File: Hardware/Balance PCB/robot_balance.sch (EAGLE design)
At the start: 49 parts, among them Q1 16Mhz

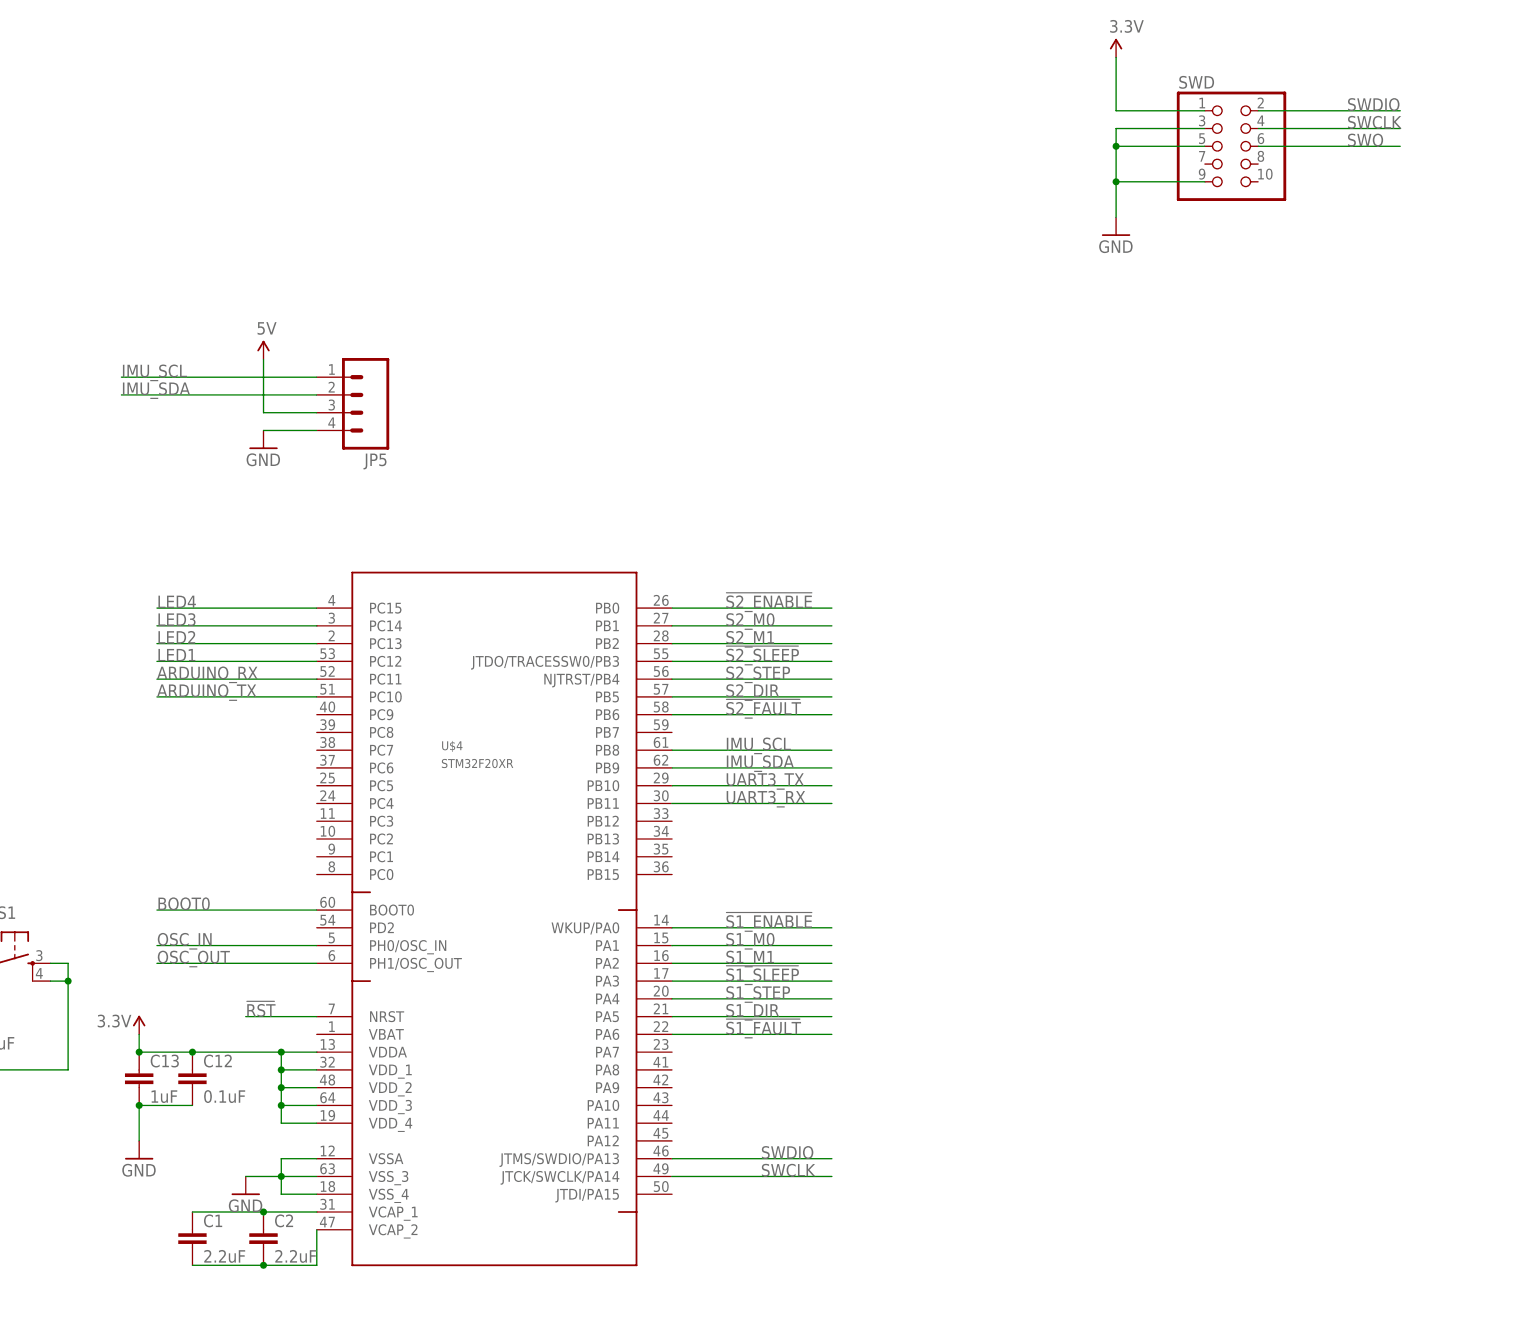
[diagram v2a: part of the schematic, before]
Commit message: Put a larger JTAG connector
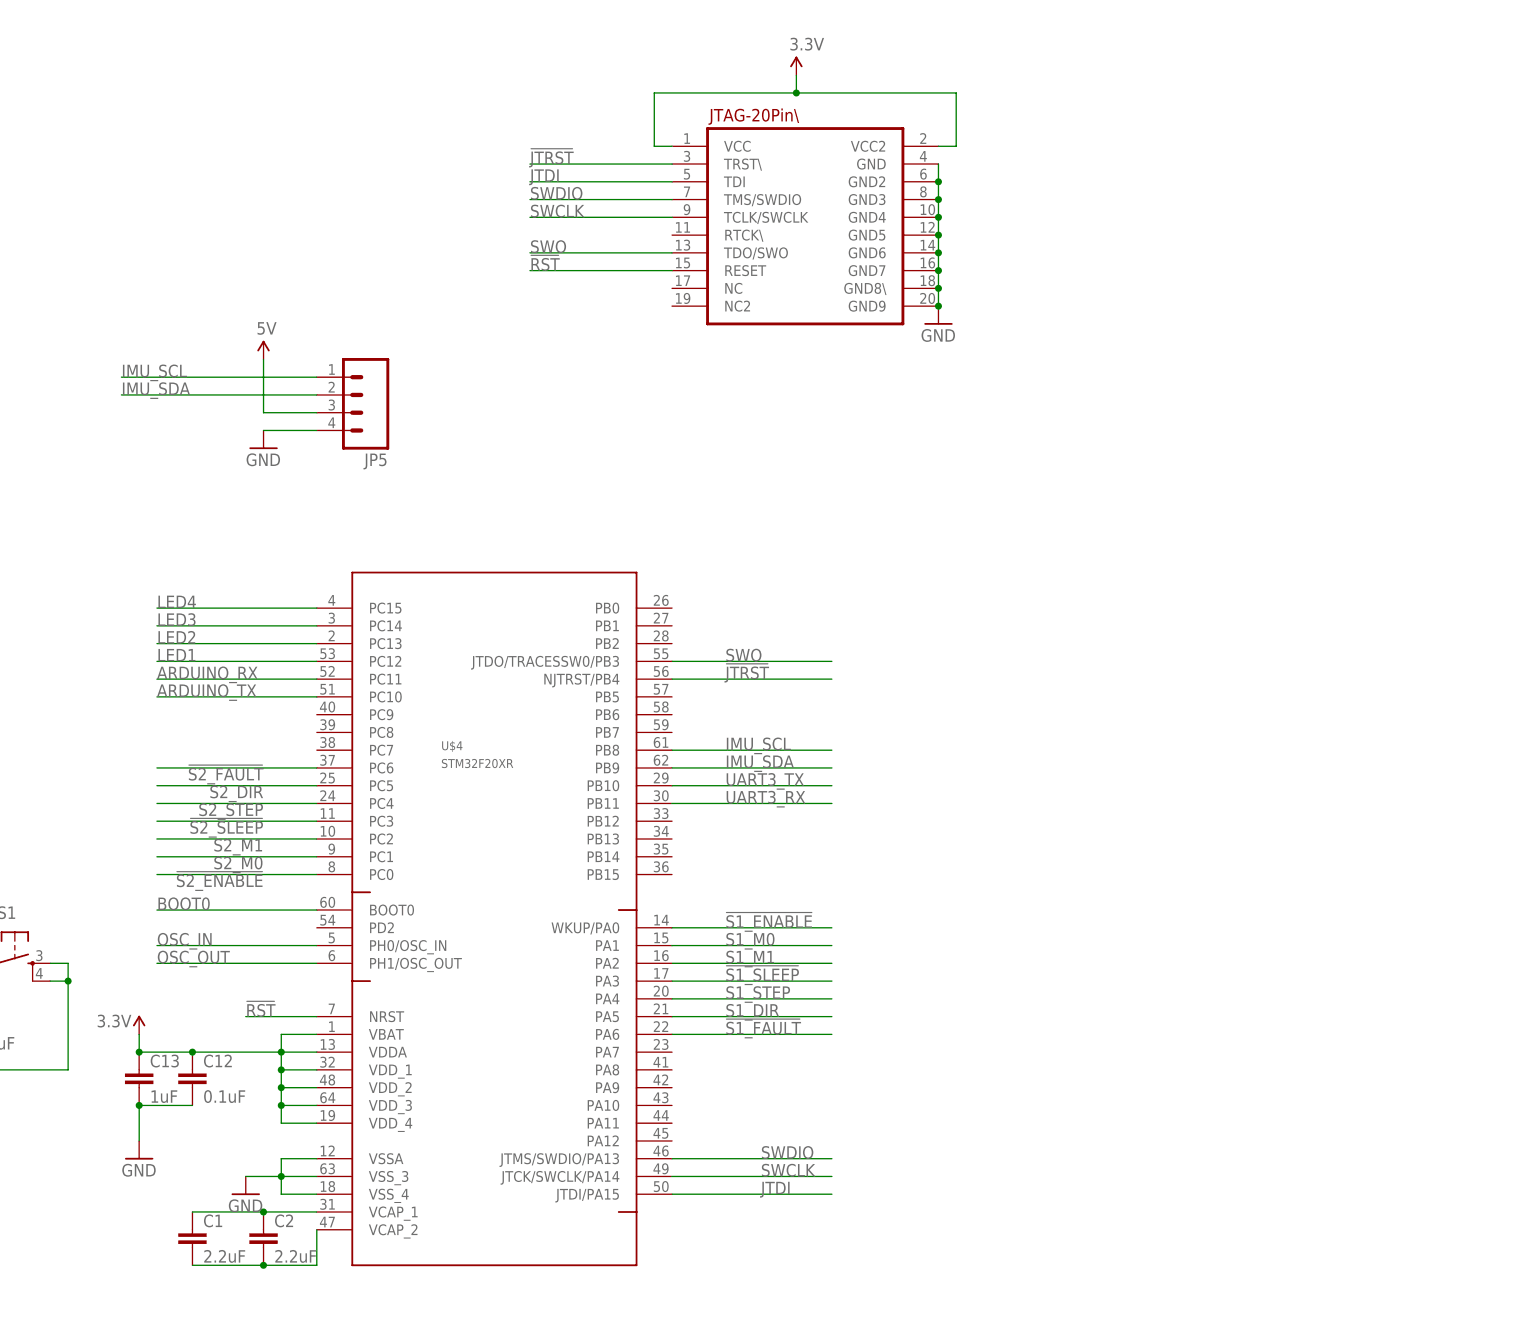
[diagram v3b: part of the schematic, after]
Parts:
- removed SWD: (no value), Sandwich:PINHD-2X5-1.27MM
- added U$2: JTAG_20PIN, JonathanLukas:JTAG_20PIN
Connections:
- new net !JTRST: U$2.TRST\, U$4.NJTRST/PB4
- new net JTDI: U$2.TDI, U$4.JTDI/PA15
- net !RST: now also U$2.RESET
- net !S2_ENABLE: now also U$4.PC0; no longer U$4.PB0
- net !S2_FAULT: now also U$4.PC6; no longer U$4.PB6
- net !S2_SLEEP: now also U$4.PC3; no longer U$4.JTDO/TRACESSW0/PB3
- net 3.3V: now also U$2.VCC, U$2.VCC2, U$4.VBAT; no longer SWD.1
- net GND: now also U$2.GND, U$2.GND2, U$2.GND3, U$2.GND4, U$2.GND5, U$2.GND6, U$2.GND7, U$2.GND8\, U$2.GND9; no longer SWD.3, SWD.5, SWD.9
- net S2_DIR: now also U$4.PC5; no longer U$4.PB5
- net S2_M0: now also U$4.PC1; no longer U$4.PB1
- net S2_M1: now also U$4.PC2; no longer U$4.PB2
- net S2_STEP: now also U$4.PC4; no longer U$4.NJTRST/PB4
- net SWCLK: now also U$2.TCLK/SWCLK; no longer SWD.4
- net SWDIO: now also U$2.TMS/SWDIO; no longer SWD.2
- net SWO: now also U$2.TDO/SWO, U$4.JTDO/TRACESSW0/PB3; no longer SWD.6

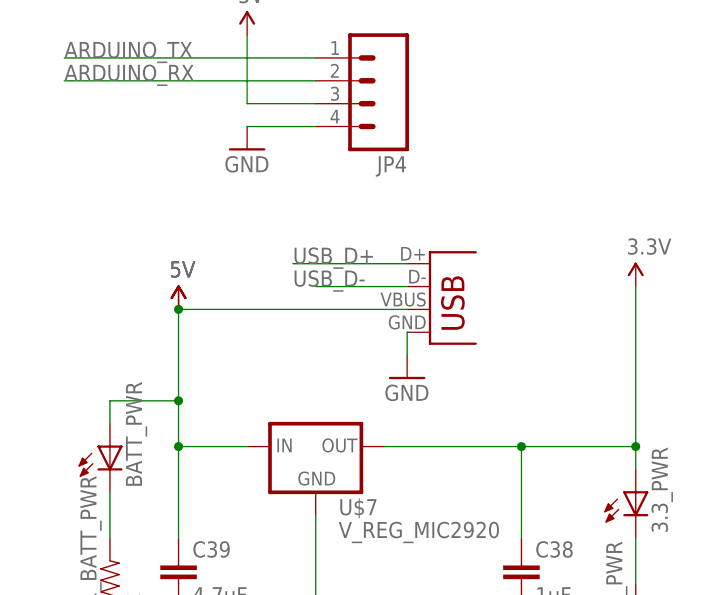
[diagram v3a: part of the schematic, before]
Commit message: Micro usb instead of Mini
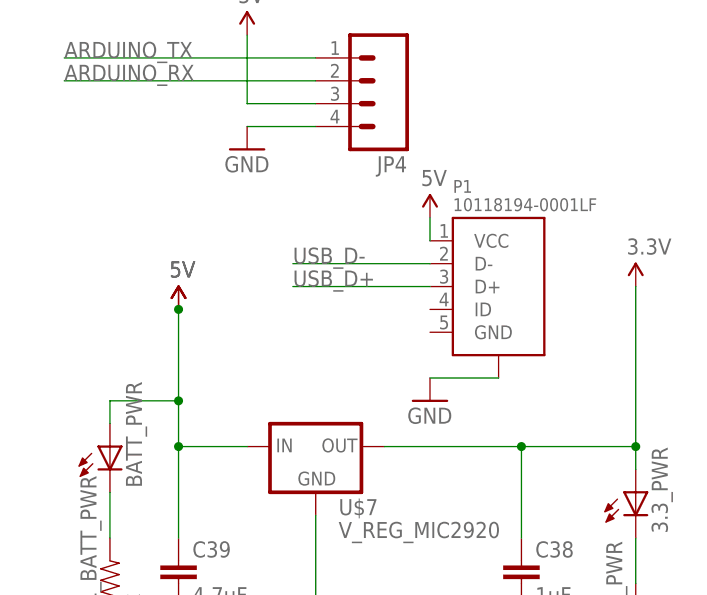
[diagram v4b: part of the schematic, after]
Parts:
- removed JP3: USBOLD, SparkFun-Connectors:USBOLD
- added P1: 10118194-0001LF, usb_micro:10118194-0001LF
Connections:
- net 5V: now also P1.VCC; no longer JP3.VBUS
- net GND: now also P1.SHIELD; no longer JP3.GND
- net USB_D+: now also P1.D+; no longer JP3.D+
- net USB_D-: now also P1.D-; no longer JP3.D-
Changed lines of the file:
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@@
 <part name="GND5" library="SparkFun-Aesthetics" deviceset="GND" device=""/>
 <part name="C4" library="SparkFun-Capacitors" deviceset="47UF-10V-10%(TANT)" device="" value="47uF"/>
-<part name="JP3" library="SparkFun-Connectors" deviceset="USB" device="OLD"/>
 <part name="GND6" library="SparkFun-Aesthetics" deviceset="GND" device=""/>
 <part name="JP4" library="SparkFun-Connectors" deviceset="M04" device="POLAR_LOCK"/>
@@
 <part name="GND12" library="SparkFun-Aesthetics" deviceset="GND" device=""/>
 <part name="SUPPLY9" library="SparkFun-Aesthetics" deviceset="3.3V" device=""/>
+<part name="P1" library="usb_micro" deviceset="10118194-0001LF" device=""/>
+<part name="SUPPLY13" library="SparkFun-Aesthetics" deviceset="5V" device=""/>
 </parts>
 <sheets>
@@
 <instance part="GND5" gate="1" x="335.28" y="-17.78"/>
 <instance part="C4" gate="G$1" x="317.5" y="-10.16"/>
-<instance part="JP3" gate="G$1" x="312.42" y="-132.08"/>
-<instance part="GND6" gate="1" x="309.88" y="-137.16"/>
+<instance part="GND6" gate="1" x="312.42" y="-139.7"/>
 <instance part="JP4" gate="G$1" x="304.8" y="-104.14" rot="R180"/>
 <instance part="GND7" gate="1" x="292.1" y="-111.76"/>
@@
 <instance part="GND12" gate="1" x="154.94" y="43.18"/>
 <instance part="SUPPLY9" gate="G$1" x="134.62" y="78.74"/>
+<instance part="P1" gate="G$1" x="317.5" y="-127"/>
+<instance part="SUPPLY13" gate="G$1" x="312.42" y="-119.38"/>
 </instances>
 <busses>
@@
 </segment>
 <segment>
-<pinref part="JP3" gate="G$1" pin="GND"/>
 <pinref part="GND6" gate="1" pin="GND"/>
-<wire x1="309.88" y1="-134.62" x2="309.88" y2="-132.08" width="0.1524" layer="91"/>
+<wire x1="312.42" y1="-137.16" x2="320.04" y2="-137.16" width="0.1524" layer="91"/>
+<pinref part="P1" gate="G$1" pin="SHIELD"/>
 </segment>
 <segment>
@@
 </segment>
 <segment>
-<wire x1="299.72" y1="-127" x2="309.88" y2="-127" width="0.1524" layer="91"/>
-<label x="297.18" y="-127" size="1.778" layer="95"/>
-<pinref part="JP3" gate="G$1" pin="D-"/>
+<wire x1="297.18" y1="-124.46" x2="312.42" y2="-124.46" width="0.1524" layer="91"/>
+<label x="297.18" y="-124.46" size="1.778" layer="95"/>
+<pinref part="P1" gate="G$1" pin="D-"/>
 </segment>
 </net>
@@
 </segment>
 <segment>
-<wire x1="297.18" y1="-124.46" x2="309.88" y2="-124.46" width="0.1524" layer="91"/>
-<label x="297.18" y="-124.46" size="1.778" layer="95"/>
-<pinref part="JP3" gate="G$1" pin="D+"/>
+<wire x1="297.18" y1="-127" x2="312.42" y2="-127" width="0.1524" layer="91"/>
+<label x="297.18" y="-127" size="1.778" layer="95"/>
+<pinref part="P1" gate="G$1" pin="D+"/>
 </segment>
 </net>
@@
 <wire x1="284.48" y1="-154.94" x2="284.48" y2="-144.78" width="0.1524" layer="91"/>
 <junction x="284.48" y="-144.78"/>
-<pinref part="JP3" gate="G$1" pin="VBUS"/>
-<wire x1="309.88" y1="-129.54" x2="284.48" y2="-129.54" width="0.1524" layer="91"/>
 <pinref part="SUPPLY5" gate="G$1" pin="5V"/>
 <junction x="284.48" y="-129.54"/>
@@
 <pinref part="SUPPLY6" gate="G$1" pin="5V"/>
 </segment>
-</net>
+<segment>
+<pinref part="P1" gate="G$1" pin="VCC"/>
+<pinref part="SUPPLY13" gate="G$1" pin="5V"/>
+<wire x1="312.42" y1="-119.38" x2="312.42" y2="-121.92" width="0.1524" layer="91"/>
+</segment>
+</net>
